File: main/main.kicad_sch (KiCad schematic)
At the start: 15 parts, among them J1 USB_C_Receptacle_USB2.0, J2 TC2030_SWD, U1 STM32F303CBTx, U2 SN74LV1T34DBV, U3 WE-TVS-82400102, U4 MIC5504-3.3YMT, Y1 16MHz

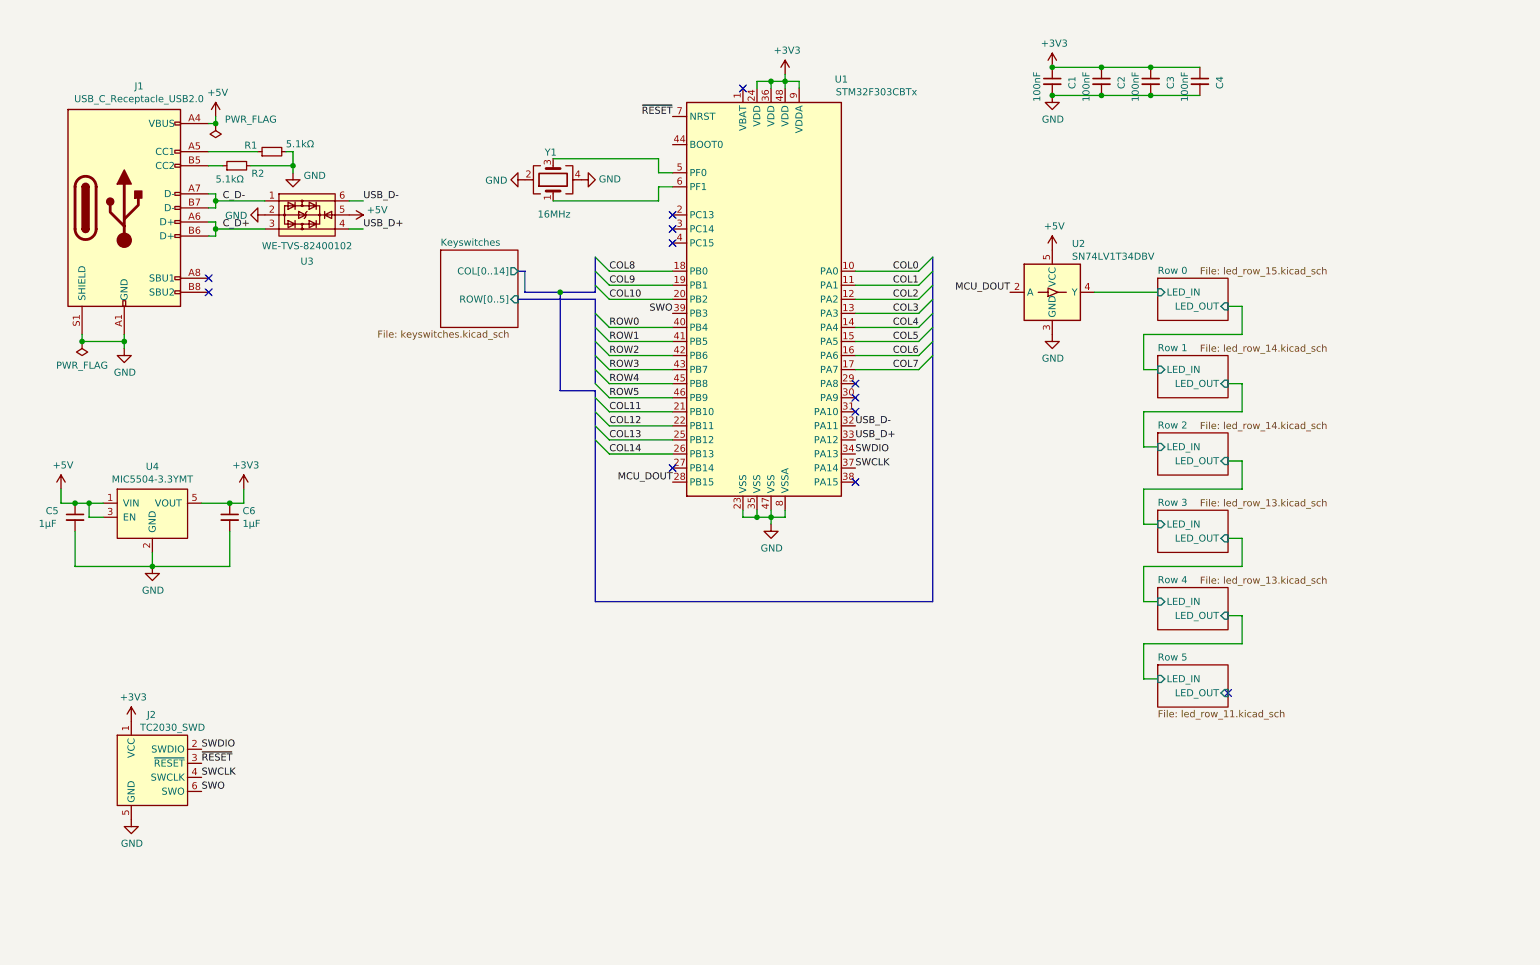
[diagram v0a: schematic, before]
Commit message: Switch to STM32L063 because I can actually buy those
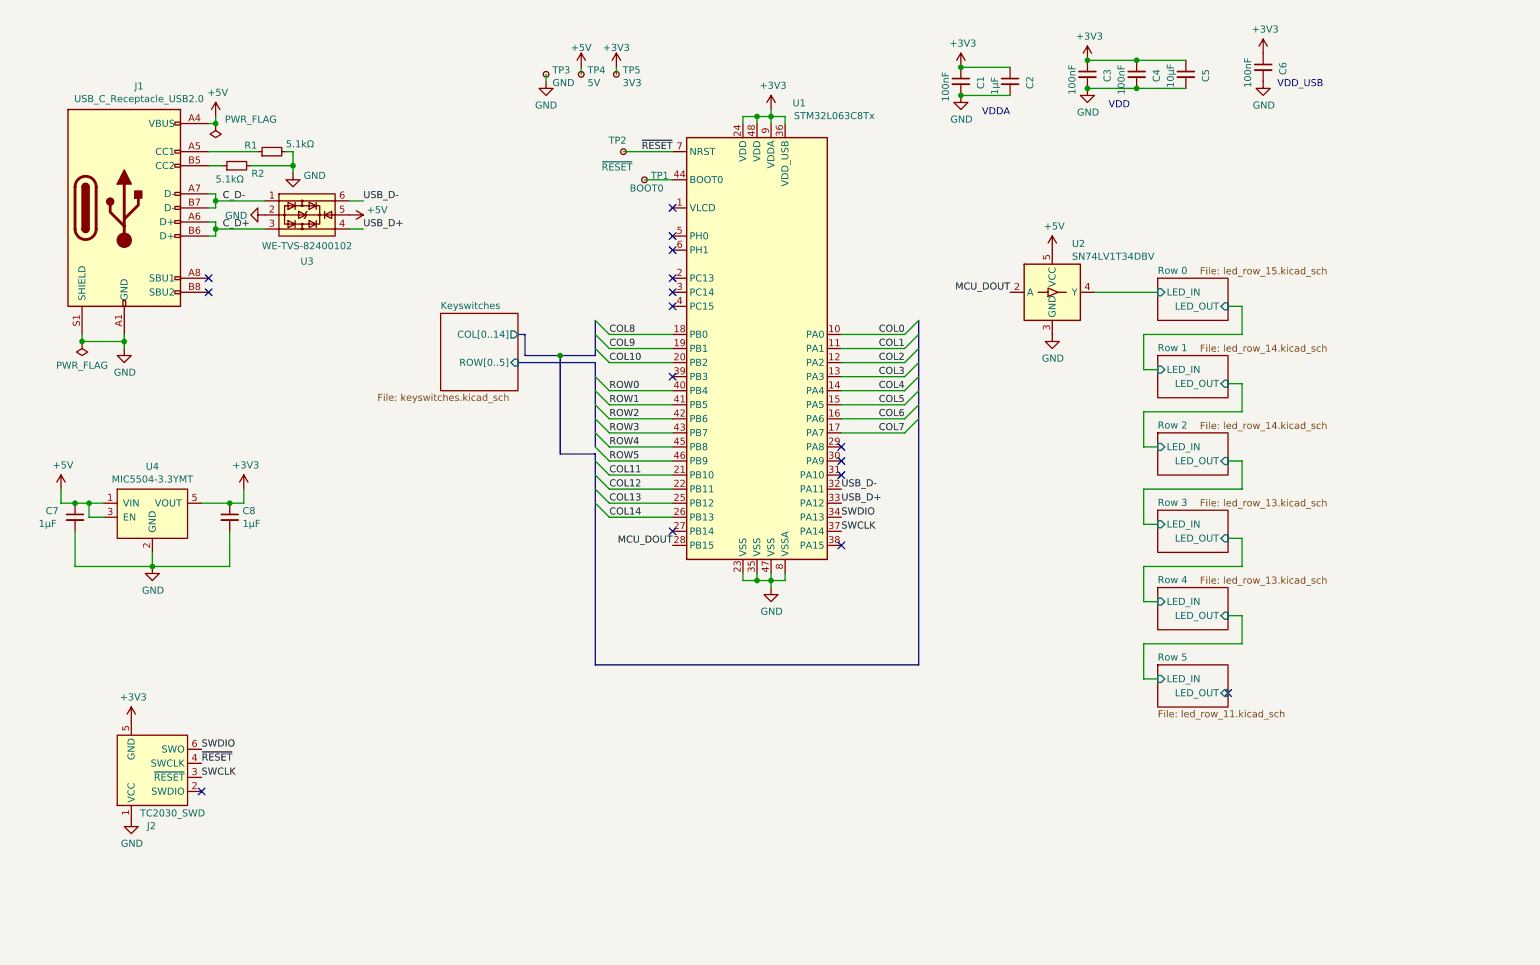
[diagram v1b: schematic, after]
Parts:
- removed U1: STM32F303CBTx, Package_QFP:LQFP-48_7x7mm_P0.5mm, symbol MCU_ST_STM32F3:STM32F303CBTx
- removed Y1: 16MHz, symbol Device:Crystal_GND24
- added C2: 1µF, Capacitor_SMD:C_0603_1608Metric, symbol Device:C_Small
- added C5: 10µF, Capacitor_SMD:C_0603_1608Metric, symbol Device:C_Small
- added TP1: BOOT0, TestPoint:TestPoint_Pad_D1.0mm, symbol Connector:TestPoint_Small
- added TP2: ~RESET, TestPoint:TestPoint_Pad_D1.0mm, symbol Connector:TestPoint_Small
- added TP3: GND, TestPoint:TestPoint_Pad_1.0x1.0mm, symbol Connector:TestPoint_Small
- added TP4: 5V, TestPoint:TestPoint_Pad_D1.0mm, symbol Connector:TestPoint_Small
- added TP5: 3V3, TestPoint:TestPoint_Pad_D1.0mm, symbol Connector:TestPoint_Small
- added U1: STM32L063C8Tx, Package_QFP:LQFP-48_7x7mm_P0.5mm, symbol MCU_ST_STM32L0:STM32L063C8Tx
- renumbered C2 to C6, C5 to C7, C6 to C8
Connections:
- net SWO is gone; now on net SWDIO: J2.6 (SWO)
- net +3V3: now also J2.5 (GND), C2.1, C5.1, TP5.1, U1.24 (VDD), U1.36 (VDD_USB), U1.48 (VDD), U1.9 (VDDA); no longer J2.1 (VCC)
- net +5V: now also TP4.1
- net COL0: now also U1.10 (PA0)
- net COL1: now also U1.11 (PA1)
- net COL10: now also U1.20 (PB2)
- net COL11: now also U1.21 (PB10)
- net COL12: now also U1.22 (PB11)
- net COL13: now also U1.25 (PB12)
- net COL14: now also U1.26 (PB13)
- net COL2: now also U1.12 (PA2)
- net COL3: now also U1.13 (PA3)
- net COL4: now also U1.14 (PA4)
- net COL5: now also U1.15 (PA5)
- net COL6: now also U1.16 (PA6)
- net COL7: now also U1.17 (PA7)
- net COL8: now also U1.18 (PB0)
- net COL9: now also U1.19 (PB1)
- net GND: now also J2.1 (VCC), C2.2, C5.2, TP3.1, U1.23 (VSS), U1.35 (VSS), U1.47 (VSS), U1.8 (VSSA); no longer J2.5 (GND)
- net MCU_DOUT: now also U1.28 (PB15)
- net ROW0: now also U1.40 (PB4)
- net ROW1: now also U1.41 (PB5)
- net ROW2: now also U1.42 (PB6)
- net ROW3: now also U1.43 (PB7)
- net ROW4: now also U1.45 (PB8)
- net ROW5: now also U1.46 (PB9)
- net SWCLK: now also J2.3 (~RESET), U1.37 (PA14); no longer J2.4 (SWCLK)
- net SWDIO: now also U1.34 (PA13); no longer J2.2 (SWDIO)
- net USB_D+: now also U1.33 (PA12)
- net USB_D-: now also U1.32 (PA11)
- net ~RESET: now also J2.4 (SWCLK), TP2.1, U1.7 (NRST); no longer J2.3 (~RESET)
- new net: TP1.1, U1.44 (BOOT0)
- no-connect marks 12 -> 16
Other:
- note added: "VDD"
- note added: "VDDA"
- note added: "VDD_USB"
- moved on the sheet: C1, C3, C4, C6

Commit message: Route all rows and columns in the matrix
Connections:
- net Row 0/LED_IN: no longer U2.4 (Y)
- new net Row 5/LED_IN: U2.4 (Y)
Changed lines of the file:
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@@
     )
   )
-  (sheet (at 222.25 60.96) (size 12.7 7.62)
+  (sheet (at 222.25 130.81) (size 12.7 7.62)
     (stroke (width 0.001) (type solid) (color 132 0 132 1))
     (fill (color 255 255 255 0.0000))
-    (property "Sheet name" "Row 0" (id 0) (at 222.25 60.3241 0)
+    (property "Sheet name" "Row 0" (id 0) (at 222.25 130.1741 0)
       (effects (font (size 1.27 1.27)) (justify left bottom))
     )
-    (property "Sheet file" "led_row_15.kicad_sch" (id 1) (at 229.87 58.9289 0)
+    (property "Sheet file" "led_row_15.kicad_sch" (id 1) (at 229.87 128.7789 0)
       (effects (font (size 1.27 1.27)) (justify left top))
     )
-    (pin "LED_OUT" input (at 234.95 66.04 0)
+    (pin "LED_OUT" input (at 234.95 135.89 0)
       (effects (font (size 1.27 1.27)) (justify right))
     )
-    (pin "LED_IN" input (at 222.25 63.5 180)
+    (pin "LED_IN" input (at 222.25 133.35 180)
+      (effects (font (size 1.27 1.27)) (justify left))
+    )
+  )
+  (sheet (at 222.25 116.84) (size 12.7 7.62)
+    (stroke (width 0.001) (type solid) (color 132 0 132 1))
+    (fill (color 255 255 255 0.0000))
+    (property "Sheet name" "Row 1" (id 0) (at 222.25 116.204 0)
+      (effects (font (size 1.27 1.27)) (justify left bottom))
+    )
+    (property "Sheet file" "led_row_14.kicad_sch" (id 1) (at 229.87 114.809 0)
+      (effects (font (size 1.27 1.27)) (justify left top))
+    )
+    (pin "LED_OUT" input (at 234.95 121.92 0)
+      (effects (font (size 1.27 1.27)) (justify right))
+    )
+    (pin "LED_IN" input (at 222.25 119.38 180)
+      (effects (font (size 1.27 1.27)) (justify left))
+    )
+  )
+  (sheet (at 222.25 102.87) (size 12.7 7.62)
+    (stroke (width 0.001) (type solid) (color 132 0 132 1))
+    (fill (color 255 255 255 0.0000))
+    (property "Sheet name" "Row 2" (id 0) (at 222.25 102.234 0)
+      (effects (font (size 1.27 1.27)) (justify left bottom))
+    )
+    (property "Sheet file" "led_row_14.kicad_sch" (id 1) (at 229.87 100.839 0)
+      (effects (font (size 1.27 1.27)) (justify left top))
+    )
+    (pin "LED_OUT" input (at 234.95 107.95 0)
+      (effects (font (size 1.27 1.27)) (justify right))
+    )
+    (pin "LED_IN" input (at 222.25 105.41 180)
+      (effects (font (size 1.27 1.27)) (justify left))
+    )
+  )
+  (sheet (at 222.25 88.9) (size 12.7 7.62)
+    (stroke (width 0.001) (type solid) (color 132 0 132 1))
+    (fill (color 255 255 255 0.0000))
+    (property "Sheet name" "Row 3" (id 0) (at 222.25 88.264 0)
+      (effects (font (size 1.27 1.27)) (justify left bottom))
+    )
+    (property "Sheet file" "led_row_13.kicad_sch" (id 1) (at 229.87 86.8689 0)
+      (effects (font (size 1.27 1.27)) (justify left top))
+    )
+    (pin "LED_OUT" input (at 234.95 93.98 0)
+      (effects (font (size 1.27 1.27)) (justify right))
+    )
+    (pin "LED_IN" input (at 222.25 91.44 180)
       (effects (font (size 1.27 1.27)) (justify left))
     )
@@
     (stroke (width 0.001) (type solid) (color 132 0 132 1))
     (fill (color 255 255 255 0.0000))
-    (property "Sheet name" "Row 1" (id 0) (at 222.25 74.294 0)
+    (property "Sheet name" "Row 4" (id 0) (at 222.25 74.294 0)
       (effects (font (size 1.27 1.27)) (justify left bottom))
     )
-    (property "Sheet file" "led_row_14.kicad_sch" (id 1) (at 229.87 72.899 0)
+    (property "Sheet file" "led_row_13.kicad_sch" (id 1) (at 229.87 72.8989 0)
       (effects (font (size 1.27 1.27)) (justify left top))
     )
@@
     )
   )
-  (sheet (at 222.25 88.9) (size 12.7 7.62)
+  (sheet (at 222.25 60.96) (size 12.7 7.62)
     (stroke (width 0.001) (type solid) (color 132 0 132 1))
     (fill (color 255 255 255 0.0000))
-    (property "Sheet name" "Row 2" (id 0) (at 222.25 88.264 0)
+    (property "Sheet name" "Row 5" (id 0) (at 222.25 60.3241 0)
       (effects (font (size 1.27 1.27)) (justify left bottom))
     )
-    (property "Sheet file" "led_row_14.kicad_sch" (id 1) (at 229.87 86.869 0)
+    (property "Sheet file" "led_row_11.kicad_sch" (id 1) (at 229.87 58.9289 0)
       (effects (font (size 1.27 1.27)) (justify left top))
     )
-    (pin "LED_OUT" input (at 234.95 93.98 0)
+    (pin "LED_OUT" input (at 234.95 66.04 0)
       (effects (font (size 1.27 1.27)) (justify right))
     )
-    (pin "LED_IN" input (at 222.25 91.44 180)
+    (pin "LED_IN" input (at 222.25 63.5 180)
       (effects (font (size 1.27 1.27)) (justify left))
     )
-  )
-  (sheet (at 222.25 102.87) (size 12.7 7.62)
-    (stroke (width 0.001) (type solid) (color 132 0 132 1))
-    (fill (color 255 255 255 0.0000))
-    (property "Sheet name" "Row 3" (id 0) (at 222.25 102.234 0)
-      (effects (font (size 1.27 1.27)) (justify left bottom))
-    )
-    (property "Sheet file" "led_row_13.kicad_sch" (id 1) (at 229.87 100.8389 0)
-      (effects (font (size 1.27 1.27)) (justify left top))
-    )
-    (pin "LED_OUT" input (at 234.95 107.95 0)
-      (effects (font (size 1.27 1.27)) (justify right))
-    )
-    (pin "LED_IN" input (at 222.25 105.41 180)
-      (effects (font (size 1.27 1.27)) (justify left))
-    )
-  )
-  (sheet (at 222.25 116.84) (size 12.7 7.62)
-    (stroke (width 0.001) (type solid) (color 132 0 132 1))
-    (fill (color 255 255 255 0.0000))
-    (property "Sheet name" "Row 4" (id 0) (at 222.25 116.204 0)
-      (effects (font (size 1.27 1.27)) (justify left bottom))
-    )
-    (property "Sheet file" "led_row_13.kicad_sch" (id 1) (at 229.87 114.8089 0)
-      (effects (font (size 1.27 1.27)) (justify left top))
-    )
-    (pin "LED_OUT" input (at 234.95 121.92 0)
-      (effects (font (size 1.27 1.27)) (justify right))
-    )
-    (pin "LED_IN" input (at 222.25 119.38 180)
-      (effects (font (size 1.27 1.27)) (justify left))
-    )
-  )
-  (sheet (at 222.25 130.81) (size 12.7 7.62)
-    (stroke (width 0.001) (type solid) (color 132 0 132 1))
-    (fill (color 255 255 255 0.0000))
-    (property "Sheet name" "Row 5" (id 0) (at 222.25 130.1741 0)
-      (effects (font (size 1.27 1.27)) (justify left bottom))
-    )
-    (property "Sheet file" "led_row_11.kicad_sch" (id 1) (at 222.25 138.9389 0)
-      (effects (font (size 1.27 1.27)) (justify left top))
-    )
-    (pin "LED_OUT" input (at 234.95 135.89 0)
-      (effects (font (size 1.27 1.27)) (justify right))
-    )
-    (pin "LED_IN" input (at 222.25 133.35 180)
-      (effects (font (size 1.27 1.27)) (justify left))
-    )

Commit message: Start appeasing the DRC
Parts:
- added H1, H2, H3, H4: MountingHole_Pad, MountingHole:MountingHole_2.2mm_M2_Pad, symbol Mechanical:MountingHole_Pad
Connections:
- net GND: now also H1.1, H2.1, H3.1, H4.1
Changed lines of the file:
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@@
   (junction (at 54.61 101.6) (diameter 1.016) (color 0 0 0 0))
   (junction (at 66.04 40.64) (diameter 1.016) (color 0 0 0 0))
+  (junction (at 104.14 156.21) (diameter 1.016) (color 0 0 0 0))
+  (junction (at 111.76 156.21) (diameter 1.016) (color 0 0 0 0))
   (junction (at 149.86 31.75) (diameter 1.016) (color 0 0 0 0))
   (junction (at 149.86 115.57) (diameter 1.016) (color 0 0 0 0))
@@
     (stroke (width 0) (type solid) (color 0 0 0 0))
   )
+  (wire (pts (xy 96.52 156.21) (xy 104.14 156.21))
+    (stroke (width 0) (type solid) (color 0 0 0 0))
+  )
+  (wire (pts (xy 104.14 156.21) (xy 111.76 156.21))
+    (stroke (width 0) (type solid) (color 0 0 0 0))
+  )
   (wire (pts (xy 111.76 24.13) (xy 111.76 25.4))
     (stroke (width 0) (type solid) (color 0 0 0 0))
   )
+  (wire (pts (xy 111.76 156.21) (xy 111.76 158.75))
+    (stroke (width 0) (type solid) (color 0 0 0 0))
+  )
+  (wire (pts (xy 111.76 156.21) (xy 119.38 156.21))
+    (stroke (width 0) (type solid) (color 0 0 0 0))
+  )
   (wire (pts (xy 118.11 22.86) (xy 118.11 24.13))
     (stroke (width 0) (type solid) (color 0 0 0 0))
@@
     (pin "1")
   )
+  (symbol (lib_id "power:GND") (at 111.76 158.75 0) (unit 1)
+    (in_bom yes) (on_board yes) (fields_autoplaced)
+    (property "Reference" "#PWR024" (id 0) (at 111.76 165.1 0)
+      (effects (font (size 1.27 1.27)) hide)
+    )
+    (property "Value" "GND" (id 1) (at 111.76 163.0744 0))
+    (property "Footprint" "" (id 2) (at 111.76 158.75 0)
+      (effects (font (size 1.27 1.27)) hide)
+    )
+    (property "Datasheet" "" (id 3) (at 111.76 158.75 0)
+      (effects (font (size 1.27 1.27)) hide)
+    )
+    (pin "1")
+  )
   (symbol (lib_id "power:GND") (at 152.4 116.84 0) (unit 1)
     (in_bom yes) (on_board yes)
@@
     (pin "2")
   )
+  (symbol (lib_id "Mechanical:MountingHole_Pad") (at 96.52 153.67 0) (unit 1)
+    (in_bom yes) (on_board yes) (fields_autoplaced)
+    (property "Reference" "H1" (id 0) (at 99.0601 152.7821 0)
+      (effects (font (size 1.27 1.27)) (justify left))
+    )
+    (property "Value" "MountingHole_Pad" (id 1) (at 99.0601 155.0808 0)
+      (effects (font (size 1.27 1.27)) (justify left) hide)
+    )
+    (property "Footprint" "MountingHole:MountingHole_2.2mm_M2_Pad" (id 2) (at 96.52 153.67 0)
+      (effects (font (size 1.27 1.27)) hide)
+    )
+    (property "Datasheet" "~" (id 3) (at 96.52 153.67 0)
+      (effects (font (size 1.27 1.27)) hide)
+    )
+    (pin "1")
+  )
+  (symbol (lib_id "Mechanical:MountingHole_Pad") (at 104.14 153.67 0) (unit 1)
+    (in_bom yes) (on_board yes) (fields_autoplaced)
+    (property "Reference" "H2" (id 0) (at 106.6801 152.7821 0)
+      (effects (font (size 1.27 1.27)) (justify left))
+    )
+    (property "Value" "MountingHole_Pad" (id 1) (at 106.6801 155.0808 0)
+      (effects (font (size 1.27 1.27)) (justify left) hide)
+    )
+    (property "Footprint" "MountingHole:MountingHole_2.2mm_M2_Pad" (id 2) (at 104.14 153.67 0)
+      (effects (font (size 1.27 1.27)) hide)
+    )
+    (property "Datasheet" "~" (id 3) (at 104.14 153.67 0)
+      (effects (font (size 1.27 1.27)) hide)
+    )
+    (pin "1")
+  )
+  (symbol (lib_id "Mechanical:MountingHole_Pad") (at 111.76 153.67 0) (unit 1)
+    (in_bom yes) (on_board yes) (fields_autoplaced)
+    (property "Reference" "H3" (id 0) (at 114.3001 152.7821 0)
+      (effects (font (size 1.27 1.27)) (justify left))
+    )
+    (property "Value" "MountingHole_Pad" (id 1) (at 114.3001 155.0808 0)
+      (effects (font (size 1.27 1.27)) (justify left) hide)
+    )
+    (property "Footprint" "MountingHole:MountingHole_2.2mm_M2_Pad" (id 2) (at 111.76 153.67 0)
+      (effects (font (size 1.27 1.27)) hide)
+    )
+    (property "Datasheet" "~" (id 3) (at 111.76 153.67 0)
+      (effects (font (size 1.27 1.27)) hide)
+    )
+    (pin "1")
+  )
+  (symbol (lib_id "Mechanical:MountingHole_Pad") (at 119.38 153.67 0) (unit 1)
+    (in_bom yes) (on_board yes) (fields_autoplaced)
+    (property "Reference" "H4" (id 0) (at 121.9201 152.7821 0)
+      (effects (font (size 1.27 1.27)) (justify left))
+    )
+    (property "Value" "MountingHole_Pad" (id 1) (at 121.9201 155.0808 0)
+      (effects (font (size 1.27 1.27)) (justify left) hide)
+    )
+    (property "Footprint" "MountingHole:MountingHole_2.2mm_M2_Pad" (id 2) (at 119.38 153.67 0)
+      (effects (font (size 1.27 1.27)) hide)
+    )
+    (property "Datasheet" "~" (id 3) (at 119.38 153.67 0)
+      (effects (font (size 1.27 1.27)) hide)
+    )
+    (pin "1")
+  )
   (symbol (lib_id "Power_Protection:WE-TVS-82400102") (at 68.58 49.53 0) (unit 1)
     (in_bom yes) (on_board yes)
@@
       (reference "#PWR023") (unit 1) (value "GND") (footprint "")
     )
+    (path "/04aab70a-7a65-4a4e-971b-0b6453ac6e87"
+      (reference "#PWR024") (unit 1) (value "GND") (footprint "")
+    )
     (path "/74378d3c-a03d-416b-9027-b1ba33a9ea3a/899e053a-131d-4ca7-b6a2-fb057ea70e53"
       (reference "#PWR0101") (unit 1) (value "+5V") (footprint "")
@@
       (reference "D180") (unit 1) (value "SK6812MINI-E") (footprint "chonc60:LED_SK6812_MINI_E_REVERSE")
     )
+    (path "/a4b901ee-bd16-4ae2-8b46-c36b4d47046a"
+      (reference "H1") (unit 1) (value "MountingHole_Pad") (footprint "MountingHole:MountingHole_2.2mm_M2_Pad")
+    )
+    (path "/6150b472-837a-4f6e-8d14-0369cb9b0aa1"
+      (reference "H2") (unit 1) (value "MountingHole_Pad") (footprint "MountingHole:MountingHole_2.2mm_M2_Pad")
+    )
+    (path "/55a0cac0-04a8-45b0-82f6-05ecc5343acc"
+      (reference "H3") (unit 1) (value "MountingHole_Pad") (footprint "MountingHole:MountingHole_2.2mm_M2_Pad")
+    )
+    (path "/fb852439-6e05-4a6c-9959-5a1f65d477bf"
+      (reference "H4") (unit 1) (value "MountingHole_Pad") (footprint "MountingHole:MountingHole_2.2mm_M2_Pad")
+    )
     (path "/5239d4b6-34d9-42bb-83ce-d22963f1ba2a"
